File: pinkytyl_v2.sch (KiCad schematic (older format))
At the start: 57 parts, among them J1 AudioJack3, J3 USB_B_Mini, J5 Conn_02x05_Odd_Even, K00 KEYSW, K10 KEYSW, K11 KEYSW, K12 KEYSW, K13 KEYSW, K14 KEYSW, K15 KEYSW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

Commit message: Inc
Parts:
- C1, C2, C3, C4, C5, C6, C7: footprint (none) -> Capacitor_SMD:C_0402_1005Metric
- D00, D10, D11, D12, D13, D14, D15, D20, D21, D22, D23, D24, D25, D30, D31, D32, D33, D34, D35, D40, D41: footprint (none) -> Diode_SMD:D_SOD-123
- J1: footprint (none) -> Connector_Audio:Jack_3.5mm_CUI_SJ-3523-SMT_Horizontal
- J3: footprint (none) -> Connector_USB:USB_Micro-B_Molex-105017-0001
- J5: footprint (none) -> Connector:Tag-Connect_TC2050-IDC-NL_2x05_P1.27mm_Vertical
- K00, K10, K11, K12, K13, K14, K15, K20, K21, K22, K23, K24, K25, K30, K31, K32, K33, K34, K35, K40, K41: footprint (none) -> Switch_Keyboard_Cherry_MX:SW_Cherry_MX_PCB_1.00u
- R1, R2, R3: footprint (none) -> Resistor_SMD:R_0402_1005Metric
- Y1: footprint (none) -> Crystal:Crystal_SMD_5032-2Pin_5.0x3.2mm

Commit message: Adds MU version and initial placing
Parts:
- removed U1: ATmega32U4RC-AU, Package_QFP:TQFP-44_10x10mm_P0.8mm, symbol MCU_Microchip_ATmega:ATmega32U4RC-AU
- added U1: ATmega32U4-MU, Package_DFN_QFN:QFN-44-1EP_7x7mm_P0.5mm_EP5.2x5.2mm, symbol MCU_Microchip_ATmega:ATmega32U4-MU
- renumbered D00 to D0, K00 to K0
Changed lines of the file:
@@
-$EndComp
-$Comp
-L MCU_Microchip_ATmega:ATmega32U4RC-AU U1
-U 1 1 6147171C
-P 2900 2700
-F 0 "U1" H 3100 900 50  0000 C CNN
-F 1 "ATmega32U4RC-AU" H 3350 800 50  0000 C CNN
-F 2 "Package_QFP:TQFP-44_10x10mm_P0.8mm" H 2900 2700 50  0001 C CIN
-F 3 "http://ww1.microchip.com/downloads/en/DeviceDoc/Atmel-7766-8-bit-AVR-ATmega16U4-32U4_Datasheet.pdf" H 2900 2700 50  0001 C CNN
-	1    2900 2700
-	1    0    0    -1
 $EndComp
 $Comp
@@
 $EndComp
 $Comp
-L keyboard_parts:KEYSW K00
+L keyboard_parts:KEYSW K0
 U 1 1 615A37F1
 P 6450 3250
-F 0 "K00" H 6450 3483 60  0000 C CNN
+F 0 "K0" H 6450 3483 60  0000 C CNN
 F 1 "KEYSW" H 6450 3150 60  0001 C CNN
 F 2 "Switch_Keyboard_Cherry_MX:SW_Cherry_MX_PCB_1.00u" H 6450 3250 60  0001 C CNN
@@
 $EndComp
 $Comp
-L Device:D D00
+L Device:D D0
 U 1 1 615F90BB
 P 6750 3100
-F 0 "D00" V 6704 3180 50  0000 L CNN
+F 0 "D0" V 6704 3180 50  0000 L CNN
 F 1 "D" V 6795 3180 50  0000 L CNN
 F 2 "Diode_SMD:D_SOD-123" H 6750 3100 50  0001 C CNN
@@
 	1    0    0    -1
 $EndComp
+$Comp
+L MCU_Microchip_ATmega:ATmega32U4-MU U1
+U 1 1 614A5BC3
+P 2900 2700
+F 0 "U1" H 2900 811 50  0000 C CNN
+F 1 "ATmega32U4-MU" H 2900 720 50  0000 C CNN
+F 2 "Package_DFN_QFN:QFN-44-1EP_7x7mm_P0.5mm_EP5.2x5.2mm" H 2900 2700 50  0001 C CIN
+F 3 "http://ww1.microchip.com/downloads/en/DeviceDoc/Atmel-7766-8-bit-AVR-ATmega16U4-32U4_Datasheet.pdf" H 2900 2700 50  0001 C CNN
+	1    2900 2700
+	1    0    0    -1
+$EndComp

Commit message: Inc
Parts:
- removed Y1: 16MHz, Crystal:Crystal_SMD_5032-2Pin_5.0x3.2mm, symbol Device:Crystal_Small
- added Y1: Crystal_GND24_Small, Crystal:Crystal_SMD_3225-4Pin_3.2x2.5mm, symbol Device:Crystal_GND24_Small
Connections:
- wire segments 77 -> 80

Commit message: DRC passing and is now double sided
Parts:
- K0, K10, K11, K12, K13, K14, K15, K20, K21, K22, K23, K24, K25, K30, K31, K32, K33, K34, K35, K40, K41: footprint Switch_Keyboard_Cherry_MX:SW_Cherry_MX_PCB_1.00u -> keyswitches:SW_MX_reversible_minimal
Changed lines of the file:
@@
 F 0 "K10" H 5550 4133 60  0000 C CNN
 F 1 "KEYSW" H 5550 3800 60  0001 C CNN
-F 2 "Switch_Keyboard_Cherry_MX:SW_Cherry_MX_PCB_1.00u" H 5550 3900 60  0001 C CNN
+F 2 "keyswitches:SW_MX_reversible_minimal" H 5550 3900 60  0001 C CNN
 F 3 "" H 5550 3900 60  0000 C CNN
 	1    5550 3900
@@
 F 0 "K11" H 6450 4133 60  0000 C CNN
 F 1 "KEYSW" H 6450 3800 60  0001 C CNN
-F 2 "Switch_Keyboard_Cherry_MX:SW_Cherry_MX_PCB_1.00u" H 6450 3900 60  0001 C CNN
+F 2 "keyswitches:SW_MX_reversible_minimal" H 6450 3900 60  0001 C CNN
 F 3 "" H 6450 3900 60  0000 C CNN
 	1    6450 3900
@@
 F 0 "K12" H 7350 4133 60  0000 C CNN
 F 1 "KEYSW" H 7350 3800 60  0001 C CNN
-F 2 "Switch_Keyboard_Cherry_MX:SW_Cherry_MX_PCB_1.00u" H 7350 3900 60  0001 C CNN
+F 2 "keyswitches:SW_MX_reversible_minimal" H 7350 3900 60  0001 C CNN
 F 3 "" H 7350 3900 60  0000 C CNN
 	1    7350 3900
@@
 F 0 "K13" H 8200 4133 60  0000 C CNN
 F 1 "KEYSW" H 8200 3800 60  0001 C CNN
-F 2 "Switch_Keyboard_Cherry_MX:SW_Cherry_MX_PCB_1.00u" H 8200 3900 60  0001 C CNN
+F 2 "keyswitches:SW_MX_reversible_minimal" H 8200 3900 60  0001 C CNN
 F 3 "" H 8200 3900 60  0000 C CNN
 	1    8200 3900
@@
 F 0 "K14" H 9050 4133 60  0000 C CNN
 F 1 "KEYSW" H 9050 3800 60  0001 C CNN
-F 2 "Switch_Keyboard_Cherry_MX:SW_Cherry_MX_PCB_1.00u" H 9050 3900 60  0001 C CNN
+F 2 "keyswitches:SW_MX_reversible_minimal" H 9050 3900 60  0001 C CNN
 F 3 "" H 9050 3900 60  0000 C CNN
 	1    9050 3900
@@
 F 0 "K15" H 10000 4133 60  0000 C CNN
 F 1 "KEYSW" H 10000 3800 60  0001 C CNN
-F 2 "Switch_Keyboard_Cherry_MX:SW_Cherry_MX_PCB_1.00u" H 10000 3900 60  0001 C CNN
+F 2 "keyswitches:SW_MX_reversible_minimal" H 10000 3900 60  0001 C CNN
 F 3 "" H 10000 3900 60  0000 C CNN
 	1    10000 3900
@@
 F 0 "K20" H 5550 4883 60  0000 C CNN
 F 1 "KEYSW" H 5550 4550 60  0001 C CNN
-F 2 "Switch_Keyboard_Cherry_MX:SW_Cherry_MX_PCB_1.00u" H 5550 4650 60  0001 C CNN
+F 2 "keyswitches:SW_MX_reversible_minimal" H 5550 4650 60  0001 C CNN
 F 3 "" H 5550 4650 60  0000 C CNN
 	1    5550 4650
@@
 F 0 "K21" H 6450 4883 60  0000 C CNN
 F 1 "KEYSW" H 6450 4550 60  0001 C CNN
-F 2 "Switch_Keyboard_Cherry_MX:SW_Cherry_MX_PCB_1.00u" H 6450 4650 60  0001 C CNN
+F 2 "keyswitches:SW_MX_reversible_minimal" H 6450 4650 60  0001 C CNN
 F 3 "" H 6450 4650 60  0000 C CNN
 	1    6450 4650
@@
 F 0 "K22" H 7350 4883 60  0000 C CNN
 F 1 "KEYSW" H 7350 4550 60  0001 C CNN
-F 2 "Switch_Keyboard_Cherry_MX:SW_Cherry_MX_PCB_1.00u" H 7350 4650 60  0001 C CNN
+F 2 "keyswitches:SW_MX_reversible_minimal" H 7350 4650 60  0001 C CNN
 F 3 "" H 7350 4650 60  0000 C CNN
 	1    7350 4650
@@
 F 0 "K23" H 8200 4883 60  0000 C CNN
 F 1 "KEYSW" H 8200 4550 60  0001 C CNN
-F 2 "Switch_Keyboard_Cherry_MX:SW_Cherry_MX_PCB_1.00u" H 8200 4650 60  0001 C CNN
+F 2 "keyswitches:SW_MX_reversible_minimal" H 8200 4650 60  0001 C CNN
 F 3 "" H 8200 4650 60  0000 C CNN
 	1    8200 4650
@@
 F 0 "K24" H 9050 4883 60  0000 C CNN
 F 1 "KEYSW" H 9050 4550 60  0001 C CNN
-F 2 "Switch_Keyboard_Cherry_MX:SW_Cherry_MX_PCB_1.00u" H 9050 4650 60  0001 C CNN
+F 2 "keyswitches:SW_MX_reversible_minimal" H 9050 4650 60  0001 C CNN
 F 3 "" H 9050 4650 60  0000 C CNN
 	1    9050 4650
@@
 F 0 "K25" H 10000 4883 60  0000 C CNN
 F 1 "KEYSW" H 10000 4550 60  0001 C CNN
-F 2 "Switch_Keyboard_Cherry_MX:SW_Cherry_MX_PCB_1.00u" H 10000 4650 60  0001 C CNN
+F 2 "keyswitches:SW_MX_reversible_minimal" H 10000 4650 60  0001 C CNN
 F 3 "" H 10000 4650 60  0000 C CNN
 	1    10000 4650
@@
 F 0 "K30" H 5550 5683 60  0000 C CNN
 F 1 "KEYSW" H 5550 5350 60  0001 C CNN
-F 2 "Switch_Keyboard_Cherry_MX:SW_Cherry_MX_PCB_1.00u" H 5550 5450 60  0001 C CNN
+F 2 "keyswitches:SW_MX_reversible_minimal" H 5550 5450 60  0001 C CNN
 F 3 "" H 5550 5450 60  0000 C CNN
 	1    5550 5450
@@
 F 0 "K31" H 6450 5683 60  0000 C CNN
 F 1 "KEYSW" H 6450 5350 60  0001 C CNN
-F 2 "Switch_Keyboard_Cherry_MX:SW_Cherry_MX_PCB_1.00u" H 6450 5450 60  0001 C CNN
+F 2 "keyswitches:SW_MX_reversible_minimal" H 6450 5450 60  0001 C CNN
 F 3 "" H 6450 5450 60  0000 C CNN
 	1    6450 5450
@@
 F 0 "K32" H 7350 5683 60  0000 C CNN
 F 1 "KEYSW" H 7350 5350 60  0001 C CNN
-F 2 "Switch_Keyboard_Cherry_MX:SW_Cherry_MX_PCB_1.00u" H 7350 5450 60  0001 C CNN
+F 2 "keyswitches:SW_MX_reversible_minimal" H 7350 5450 60  0001 C CNN
 F 3 "" H 7350 5450 60  0000 C CNN
 	1    7350 5450
@@
 F 0 "K33" H 8200 5683 60  0000 C CNN
 F 1 "KEYSW" H 8200 5350 60  0001 C CNN
-F 2 "Switch_Keyboard_Cherry_MX:SW_Cherry_MX_PCB_1.00u" H 8200 5450 60  0001 C CNN
+F 2 "keyswitches:SW_MX_reversible_minimal" H 8200 5450 60  0001 C CNN
 F 3 "" H 8200 5450 60  0000 C CNN
 	1    8200 5450
@@
 F 0 "K34" H 9050 5683 60  0000 C CNN
 F 1 "KEYSW" H 9050 5350 60  0001 C CNN
-F 2 "Switch_Keyboard_Cherry_MX:SW_Cherry_MX_PCB_1.00u" H 9050 5450 60  0001 C CNN
+F 2 "keyswitches:SW_MX_reversible_minimal" H 9050 5450 60  0001 C CNN
 F 3 "" H 9050 5450 60  0000 C CNN
 	1    9050 5450
@@
 F 0 "K35" H 10000 5683 60  0000 C CNN
 F 1 "KEYSW" H 10000 5350 60  0001 C CNN
-F 2 "Switch_Keyboard_Cherry_MX:SW_Cherry_MX_PCB_1.00u" H 10000 5450 60  0001 C CNN
+F 2 "keyswitches:SW_MX_reversible_minimal" H 10000 5450 60  0001 C CNN
 F 3 "" H 10000 5450 60  0000 C CNN
 	1    10000 5450
@@
 F 0 "K40" H 9050 6383 60  0000 C CNN
 F 1 "KEYSW" H 9050 6050 60  0001 C CNN
-F 2 "Switch_Keyboard_Cherry_MX:SW_Cherry_MX_PCB_1.00u" H 9050 6150 60  0001 C CNN
+F 2 "keyswitches:SW_MX_reversible_minimal" H 9050 6150 60  0001 C CNN
 F 3 "" H 9050 6150 60  0000 C CNN
 	1    9050 6150
@@
 F 0 "K41" H 10000 6383 60  0000 C CNN
 F 1 "KEYSW" H 10000 6050 60  0001 C CNN
-F 2 "Switch_Keyboard_Cherry_MX:SW_Cherry_MX_PCB_1.00u" H 10000 6150 60  0001 C CNN
+F 2 "keyswitches:SW_MX_reversible_minimal" H 10000 6150 60  0001 C CNN
 F 3 "" H 10000 6150 60  0000 C CNN
 	1    10000 6150
@@
 F 0 "K0" H 6450 3483 60  0000 C CNN
 F 1 "KEYSW" H 6450 3150 60  0001 C CNN
-F 2 "Switch_Keyboard_Cherry_MX:SW_Cherry_MX_PCB_1.00u" H 6450 3250 60  0001 C CNN
+F 2 "keyswitches:SW_MX_reversible_minimal" H 6450 3250 60  0001 C CNN
 F 3 "" H 6450 3250 60  0000 C CNN
 	1    6450 3250

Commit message: Adds smaller version of the 3.5mm connector
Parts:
- removed J1: AudioJack3, Connector_Audio:Jack_3.5mm_CUI_SJ-3523-SMT_Horizontal, symbol Connector:AudioJack3
- added J1: STX-3501-3N, STX35013N, symbol STX-3501-3N:STX-3501-3N
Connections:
- wire segments 80 -> 83
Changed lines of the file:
@@
 	1    0    0    -1
-$EndComp
-$Comp
-L Connector:AudioJack3 J1
-U 1 1 614F8A2A
-P 5100 2550
-F 0 "J1" H 4820 2483 50  0000 R CNN
-F 1 "AudioJack3" H 4820 2574 50  0000 R CNN
-F 2 "Connector_Audio:Jack_3.5mm_CUI_SJ-3523-SMT_Horizontal" H 5100 2550 50  0001 C CNN
-F 3 "~" H 5100 2550 50  0001 C CNN
-	1    5100 2550
-	-1   0    0    1
 $EndComp
 Text GLabel 5350 1150 2    50   Input ~ 0
@@
 	1900 1300 2100 1300
 Connection ~ 2100 1300
+$Comp
+L STX-3501-3N:STX-3501-3N J1
+U 1 1 615C1FA9
+P 4900 2550
+F 0 "J1" H 5300 2817 50  0000 C CNN
+F 1 "STX-3501-3N" H 5300 2726 50  0000 C CNN
+F 2 "STX35013N" H 4900 2550 50  0001 L BNN
+F 3 "" H 4900 2550 50  0001 L BNN
+F 4 "Kycon, Inc." H 4900 2550 50  0001 L BNN "Manufacturer_Name"
+F 5 "" H 4900 2550 50  0001 L BNN "Arrow_Price-Stock"
+F 6 "STX-3501-3N" H 4900 2550 50  0001 L BNN "Manufacturer_Part_Number"
+F 7 "" H 4900 2550 50  0001 L BNN "Arrow_Part_Number"
+F 8 "Phone Connectors 3.5mm S LUGS STEREO 3P THRU HOLE" H 4900 2550 50  0001 L BNN "Description"
+F 9 "5mm" H 4900 2550 50  0001 L BNN "Height"
+F 10 "" H 4900 2550 50  0001 L BNN "Mouser_Price-Stock"
+F 11 "" H 4900 2550 50  0001 L BNN "Mouser_Part_Number"
+	1    4900 2550
+	1    0    0    -1
+$EndComp
+Wire Wire Line
+	5700 2550 5700 2200
+Wire Wire Line
+	5700 2200 4900 2200
+Wire Wire Line
+	4900 2200 4900 2450
 $EndSCHEMATC

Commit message: Cound be final
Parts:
- added J2: Conn_01x02, Connector_PinHeader_1.27mm:PinHeader_1x02_P1.27mm_Vertical, symbol Connector_Generic:Conn_01x02
- J1: footprint STX35013N -> STX-3501-3N:STX35013N
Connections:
- net GND: now also J2.2 (Pin_2)
- net reset: now also J2.1 (Pin_1)
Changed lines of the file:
@@
 F 0 "J1" H 5300 2817 50  0000 C CNN
 F 1 "STX-3501-3N" H 5300 2726 50  0000 C CNN
-F 2 "STX35013N" H 4900 2550 50  0001 L BNN
+F 2 "STX-3501-3N:STX35013N" H 4900 2550 50  0001 L BNN
 F 3 "" H 4900 2550 50  0001 L BNN
 F 4 "Kycon, Inc." H 4900 2550 50  0001 L BNN "Manufacturer_Name"
@@
 Wire Wire Line
 	4900 2200 4900 2450
+$Comp
+L Connector_Generic:Conn_01x02 J2
+U 1 1 615E9C63
+P 6500 1150
+F 0 "J2" H 6580 1142 50  0000 L CNN
+F 1 "Conn_01x02" H 6580 1051 50  0000 L CNN
+F 2 "Connector_PinHeader_1.27mm:PinHeader_1x02_P1.27mm_Vertical" H 6500 1150 50  0001 C CNN
+F 3 "~" H 6500 1150 50  0001 C CNN
+	1    6500 1150
+	1    0    0    -1
+$EndComp
+$Comp
+L power:GND #PWR04
+U 1 1 615F1A7D
+P 6300 1250
+F 0 "#PWR04" H 6300 1000 50  0001 C CNN
+F 1 "GND" H 6305 1077 50  0000 C CNN
+F 2 "" H 6300 1250 50  0001 C CNN
+F 3 "" H 6300 1250 50  0001 C CNN
+	1    6300 1250
+	1    0    0    -1
+$EndComp
+Text GLabel 6300 1150 0    50   Input ~ 0
+reset
 $EndSCHEMATC

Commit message: In the middle of slim redesign
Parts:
- removed J1: STX-3501-3N, STX-3501-3N:STX35013N, symbol STX-3501-3N:STX-3501-3N
- added J1: 50-00174, misc:54-00174, symbol misc:50-00174
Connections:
- net GND: now also J1.4
- net VCC: now also J1.1
- net serial: now also J1.2, J1.3
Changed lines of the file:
@@
 	1    0    0    -1
 $EndComp
-Text GLabel 4900 2450 0    50   Input ~ 0
+Text GLabel 5800 2350 2    50   Input ~ 0
 serial
 $Comp
 L power:VCC #PWR0114
 U 1 1 614F8A38
-P 4800 2550
-F 0 "#PWR0114" H 4800 2400 50  0001 C CNN
-F 1 "VCC" V 4815 2677 50  0000 L CNN
-F 2 "" H 4800 2550 50  0001 C CNN
-F 3 "" H 4800 2550 50  0001 C CNN
-	1    4800 2550
-	0    -1   -1   0
+P 5800 2250
+F 0 "#PWR0114" H 5800 2100 50  0001 C CNN
+F 1 "VCC" V 5815 2377 50  0000 L CNN
+F 2 "" H 5800 2250 50  0001 C CNN
+F 3 "" H 5800 2250 50  0001 C CNN
+	1    5800 2250
+	0    1    1    0
 $EndComp
 $Comp
 L power:GND #PWR0113
 U 1 1 614F8A30
-P 4800 2700
-F 0 "#PWR0113" H 4800 2450 50  0001 C CNN
-F 1 "GND" H 4805 2527 50  0000 C CNN
-F 2 "" H 4800 2700 50  0001 C CNN
-F 3 "" H 4800 2700 50  0001 C CNN
-	1    4800 2700
-	1    0    0    -1
+P 5800 2550
+F 0 "#PWR0113" H 5800 2300 50  0001 C CNN
+F 1 "GND" H 5805 2377 50  0000 C CNN
+F 2 "" H 5800 2550 50  0001 C CNN
+F 3 "" H 5800 2550 50  0001 C CNN
+	1    5800 2550
+	0    -1   -1   0
 $EndComp
 Text GLabel 5350 1150 2    50   Input ~ 0
@@
 	2200 1200 2150 1200
 Wire Wire Line
-	4900 2550 4800 2550
-Wire Wire Line
-	4800 2650 4800 2700
-Wire Wire Line
-	4900 2650 4800 2650
-Wire Wire Line
 	5050 1450 4950 1450
 Connection ~ 4950 1450
@@
 Connection ~ 2100 1300
 $Comp
-L STX-3501-3N:STX-3501-3N J1
-U 1 1 615C1FA9
-P 4900 2550
-F 0 "J1" H 5300 2817 50  0000 C CNN
-F 1 "STX-3501-3N" H 5300 2726 50  0000 C CNN
-F 2 "STX-3501-3N:STX35013N" H 4900 2550 50  0001 L BNN
-F 3 "" H 4900 2550 50  0001 L BNN
-F 4 "Kycon, Inc." H 4900 2550 50  0001 L BNN "Manufacturer_Name"
-F 5 "" H 4900 2550 50  0001 L BNN "Arrow_Price-Stock"
-F 6 "STX-3501-3N" H 4900 2550 50  0001 L BNN "Manufacturer_Part_Number"
-F 7 "" H 4900 2550 50  0001 L BNN "Arrow_Part_Number"
-F 8 "Phone Connectors 3.5mm S LUGS STEREO 3P THRU HOLE" H 4900 2550 50  0001 L BNN "Description"
-F 9 "5mm" H 4900 2550 50  0001 L BNN "Height"
-F 10 "" H 4900 2550 50  0001 L BNN "Mouser_Price-Stock"
-F 11 "" H 4900 2550 50  0001 L BNN "Mouser_Part_Number"
-	1    4900 2550
-	1    0    0    -1
-$EndComp
-Wire Wire Line
-	5700 2550 5700 2200
-Wire Wire Line
-	5700 2200 4900 2200
-Wire Wire Line
-	4900 2200 4900 2450
-$Comp
 L Connector_Generic:Conn_01x02 J2
 U 1 1 615E9C63
@@
 Text GLabel 6300 1150 0    50   Input ~ 0
 reset
+$Comp
+L misc:50-00174 J1
+U 1 1 614D3F66
+P 5800 2100
+F 0 "J1" H 5683 2215 50  0000 C CNN
+F 1 "50-00174" H 5683 2124 50  0000 C CNN
+F 2 "misc:54-00174" H 5800 2100 50  0001 C CNN
+F 3 "" H 5800 2100 50  0001 C CNN
+	1    5800 2100
+	1    0    0    -1
+$EndComp
+Wire Wire Line
+	5800 2450 5800 2350
 $EndSCHEMATC

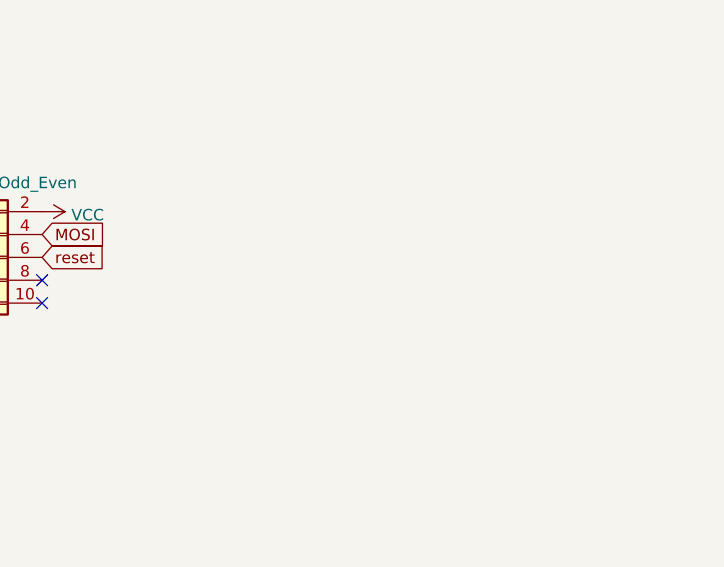
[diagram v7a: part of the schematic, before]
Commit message: Adds mounting holes
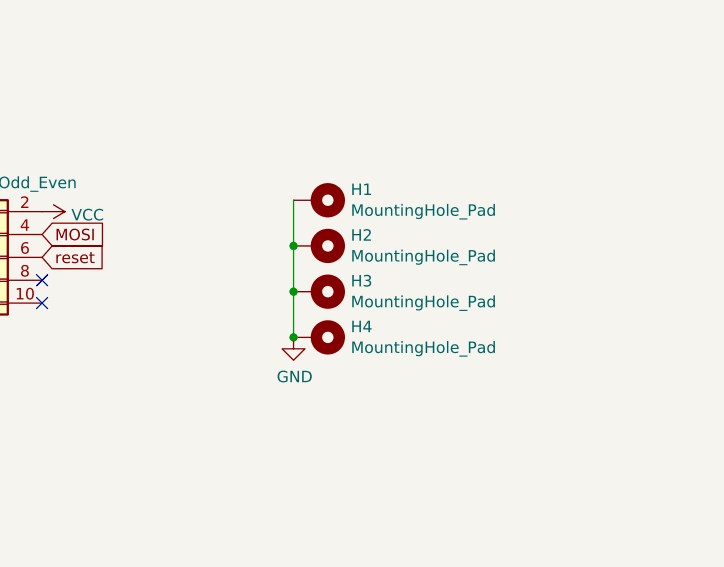
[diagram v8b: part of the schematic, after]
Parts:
- added H1, H2, H3, H4: MountingHole_Pad, MountingHole:MountingHole_2.2mm_M2_Pad, symbol Mechanical:MountingHole_Pad
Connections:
- net GND: now also H1.1, H2.1, H3.1, H4.1
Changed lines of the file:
@@
 Wire Wire Line
 	5800 2450 5800 2350
+$Comp
+L Mechanical:MountingHole_Pad H1
+U 1 1 61566A23
+P 8850 1700
+F 0 "H1" V 8804 1850 50  0000 L CNN
+F 1 "MountingHole_Pad" V 8895 1850 50  0000 L CNN
+F 2 "MountingHole:MountingHole_2.2mm_M2_Pad" H 8850 1700 50  0001 C CNN
+F 3 "~" H 8850 1700 50  0001 C CNN
+	1    8850 1700
+	0    1    1    0
+$EndComp
+$Comp
+L Mechanical:MountingHole_Pad H2
+U 1 1 615686EB
+P 8850 1900
+F 0 "H2" V 8804 2050 50  0000 L CNN
+F 1 "MountingHole_Pad" V 8895 2050 50  0000 L CNN
+F 2 "MountingHole:MountingHole_2.2mm_M2_Pad" H 8850 1900 50  0001 C CNN
+F 3 "~" H 8850 1900 50  0001 C CNN
+	1    8850 1900
+	0    1    1    0
+$EndComp
+$Comp
+L Mechanical:MountingHole_Pad H3
+U 1 1 61568EE3
+P 8850 2100
+F 0 "H3" V 8804 2250 50  0000 L CNN
+F 1 "MountingHole_Pad" V 8895 2250 50  0000 L CNN
+F 2 "MountingHole:MountingHole_2.2mm_M2_Pad" H 8850 2100 50  0001 C CNN
+F 3 "~" H 8850 2100 50  0001 C CNN
+	1    8850 2100
+	0    1    1    0
+$EndComp
+$Comp
+L Mechanical:MountingHole_Pad H4
+U 1 1 61569881
+P 8850 2300
+F 0 "H4" V 8804 2450 50  0000 L CNN
+F 1 "MountingHole_Pad" V 8895 2450 50  0000 L CNN
+F 2 "MountingHole:MountingHole_2.2mm_M2_Pad" H 8850 2300 50  0001 C CNN
+F 3 "~" H 8850 2300 50  0001 C CNN
+	1    8850 2300
+	0    1    1    0
+$EndComp
+Wire Wire Line
+	8750 1700 8750 1900
+Wire Wire Line
+	8750 2100 8750 1900
+Connection ~ 8750 1900
+Wire Wire Line
+	8750 2100 8750 2300
+Connection ~ 8750 2100
+$Comp
+L power:GND #PWR05
+U 1 1 615705C4
+P 8750 2300
+F 0 "#PWR05" H 8750 2050 50  0001 C CNN
+F 1 "GND" H 8755 2127 50  0000 C CNN
+F 2 "" H 8750 2300 50  0001 C CNN
+F 3 "" H 8750 2300 50  0001 C CNN
+	1    8750 2300
+	1    0    0    -1
+$EndComp
+Connection ~ 8750 2300
 $EndSCHEMATC
